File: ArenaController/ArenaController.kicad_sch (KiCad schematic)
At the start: 26 parts, among them J1 RJ45, J2 RJ45, J4 RJ45, J5 RJ45, J6 RJ45, J9 Barrel_Jack_MountingPin, Q1 FS3400, Q2 FS3400, Q3 FS3400, Q4 FS3400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

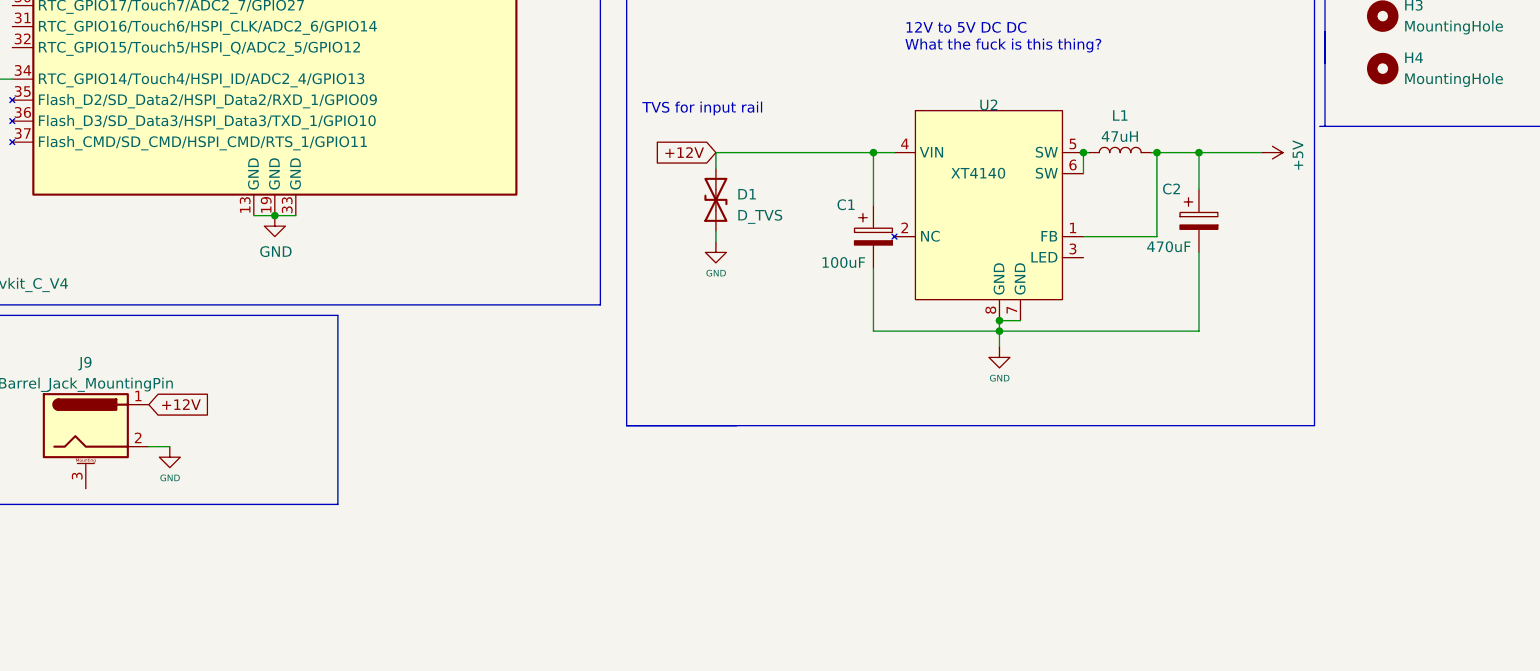
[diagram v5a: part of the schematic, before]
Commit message: Added test points and 3D model for pin headers to the ESP32 footprint.
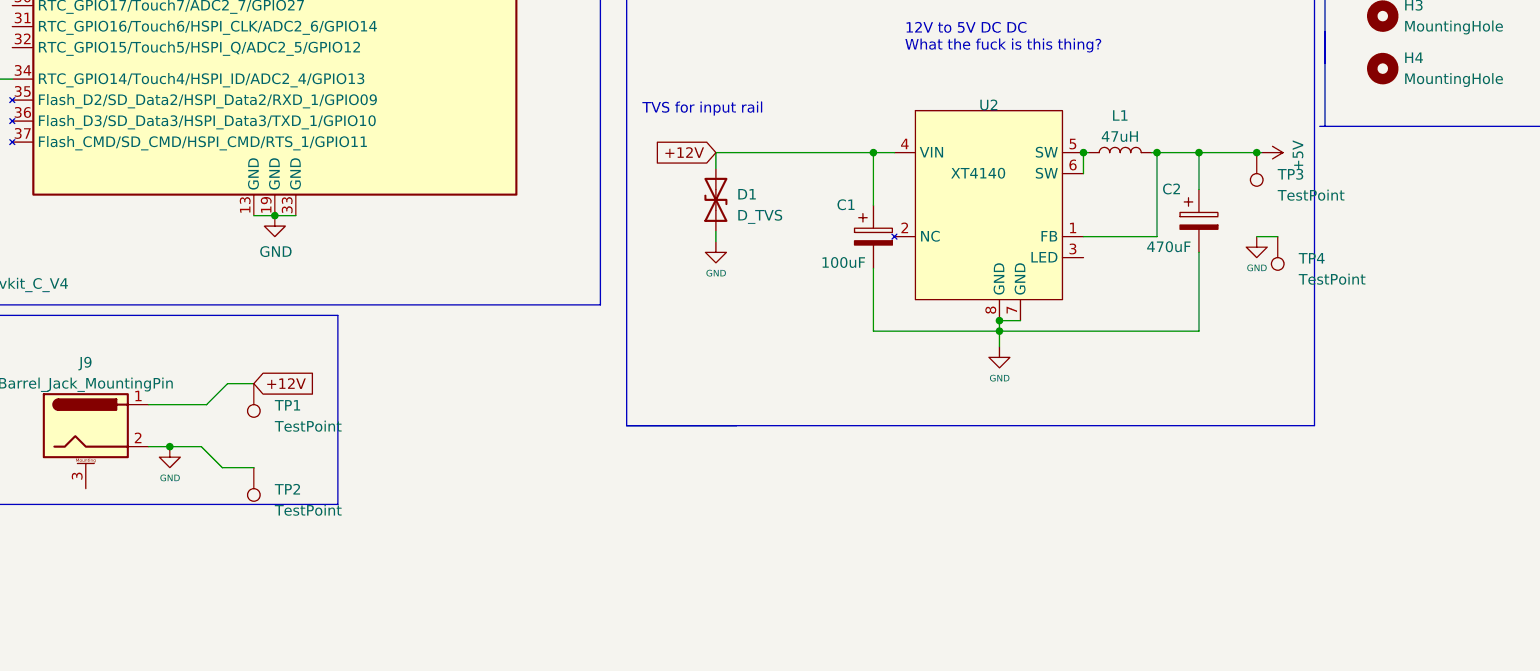
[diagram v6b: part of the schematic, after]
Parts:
- added TP1, TP2, TP3, TP4: TestPoint, TestPoint:TestPoint_Loop_D1.80mm_Drill1.0mm_Beaded, symbol Connector:TestPoint
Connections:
- net +12V: now also TP1.1
- net +5V: now also TP3.1
- net GND: now also TP2.1, TP4.1
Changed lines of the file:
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@@
   (title_block
     (title "Combat Arena Timing Control")
-    (date "2023-04-29")
-    (rev "0.5")
+    (date "2023-06-18")
+    (rev "0.6")
     (company "Fair Use Building & Research Labs, 501c3")
     (comment 2 "Neil Flynn")
@@
   (junction (at 172.085 123.825) (diameter 0) (color 0 0 0 0)
   )
+  (junction (at 47.625 159.385) (diameter 0) (color 0 0 0 0)
+  )
   (junction (at 147.955 144.145) (diameter 0) (color 0 0 0 0)
   )
   (junction (at 60.325 131.445) (diameter 0) (color 0 0 0 0)
   )
+  (junction (at 179.07 123.825) (diameter 0) (color 0 0 0 0)
+  )
   (junction (at 132.715 123.825) (diameter 0) (color 0 0 0 0)
   )
@@
     (stroke (width 0) (type default))
   )
-  (wire (pts (xy 172.085 123.825) (xy 179.705 123.825))
+  (wire (pts (xy 172.085 123.825) (xy 179.07 123.825))
     (stroke (width 0) (type default))
   )
@@
     (stroke (width 0) (type default))
   )
+  (wire (pts (xy 179.07 133.985) (xy 181.61 133.985))
+    (stroke (width 0) (type default))
+  )
   (wire (pts (xy 132.715 145.415) (xy 147.955 145.415))
     (stroke (width 0) (type default))
@@
     (stroke (width 0) (type default))
   )
+  (wire (pts (xy 53.975 161.925) (xy 57.785 161.925))
+    (stroke (width 0) (type default))
+  )
   (polyline (pts (xy 102.87 104.775) (xy 186.055 104.775))
     (stroke (width 0) (type default))
   )
+  (wire (pts (xy 54.61 151.765) (xy 57.785 151.765))
+    (stroke (width 0) (type default))
+  )
   (polyline (pts (xy 187.325 15.24) (xy 187.325 62.23))
     (stroke (width 0) (type default))
@@
     (stroke (width 0) (type default))
   )
+  (wire (pts (xy 47.625 159.385) (xy 51.435 159.385))
+    (stroke (width 0) (type default))
+  )
+  (wire (pts (xy 45.085 154.305) (xy 52.07 154.305))
+    (stroke (width 0) (type default))
+  )
   (polyline (pts (xy 187.325 113.03) (xy 187.325 109.22))
     (stroke (width 0) (type default))
@@
     (stroke (width 0) (type default))
   )
+  (wire (pts (xy 52.07 154.305) (xy 54.61 151.765))
+    (stroke (width 0) (type default))
+  )
   (polyline (pts (xy 118.11 102.87) (xy 153.67 102.87))
     (stroke (width 0) (type default))
@@
     (stroke (width 0) (type default))
   )
+  (wire (pts (xy 179.07 123.825) (xy 179.705 123.825))
+    (stroke (width 0) (type default))
+  )
   (wire (pts (xy 170.18 57.15) (xy 168.91 57.15))
     (stroke (width 0) (type default))
   )
   (wire (pts (xy 26.035 74.295) (xy 28.575 74.295))
+    (stroke (width 0) (type default))
+  )
+  (wire (pts (xy 51.435 159.385) (xy 53.975 161.925))
     (stroke (width 0) (type default))
   )
@@
     )
   )
-  (global_label "+12V" (shape input) (at 45.085 154.305 0) (fields_autoplaced)
+  (global_label "+12V" (shape input) (at 57.785 151.765 0) (fields_autoplaced)
     (effects (font (size 1.27 1.27)) (justify left))
-    (property "Intersheetrefs" "${INTERSHEET_REFS}" (at 52.4892 154.3844 0)
+    (property "Intersheetrefs" "${INTERSHEET_REFS}" (at 65.1892 151.8444 0)
       (effects (font (size 1.27 1.27)) (justify left) hide)
     )
@@
     )
   )
+  (symbol (lib_id "Connector:TestPoint") (at 179.07 123.825 180) (unit 1)
+    (in_bom yes) (on_board yes) (dnp no) (fields_autoplaced)
+    (property "Reference" "TP3" (at 181.61 126.492 0)
+      (effects (font (size 1.27 1.27)) (justify right))
+    )
+    (property "Value" "TestPoint" (at 181.61 129.032 0)
+      (effects (font (size 1.27 1.27)) (justify right))
+    )
+    (property "Footprint" "TestPoint:TestPoint_Loop_D1.80mm_Drill1.0mm_Beaded" (at 173.99 123.825 0)
+      (effects (font (size 1.27 1.27)) hide)
+    )
+    (property "Datasheet" "~" (at 173.99 123.825 0)
+      (effects (font (size 1.27 1.27)) hide)
+    )
+    (pin "1")
+    (instances
+      (project "ArenaController"
+        (path "/156576da-4c7a-4c71-af43-7540e3a24bd3"
+          (reference "TP3") (unit 1)
+        )
+      )
+    )
+  )
   (symbol (lib_id "Device:D_TVS") (at 113.665 129.54 90) (unit 1)
     (in_bom yes) (on_board yes) (dnp no) (fields_autoplaced)
@@
         (path "/156576da-4c7a-4c71-af43-7540e3a24bd3"
           (reference "R5") (unit 1)
+        )
+      )
+    )
+  )
+  (symbol (lib_id "Connector:TestPoint") (at 57.785 161.925 180) (unit 1)
+    (in_bom yes) (on_board yes) (dnp no) (fields_autoplaced)
+    (property "Reference" "TP2" (at 60.325 164.592 0)
+      (effects (font (size 1.27 1.27)) (justify right))
+    )
+    (property "Value" "TestPoint" (at 60.325 167.132 0)
+      (effects (font (size 1.27 1.27)) (justify right))
+    )
+    (property "Footprint" "TestPoint:TestPoint_Loop_D1.80mm_Drill1.0mm_Beaded" (at 52.705 161.925 0)
+      (effects (font (size 1.27 1.27)) hide)
+    )
+    (property "Datasheet" "~" (at 52.705 161.925 0)
+      (effects (font (size 1.27 1.27)) hide)
+    )
+    (pin "1")
+    (instances
+      (project "ArenaController"
+        (path "/156576da-4c7a-4c71-af43-7540e3a24bd3"
+          (reference "TP2") (unit 1)
         )
       )
@@
     )
   )
+  (symbol (lib_id "Connector:TestPoint") (at 181.61 133.985 180) (unit 1)
+    (in_bom yes) (on_board yes) (dnp no) (fields_autoplaced)
+    (property "Reference" "TP4" (at 184.15 136.652 0)
+      (effects (font (size 1.27 1.27)) (justify right))
+    )
+    (property "Value" "TestPoint" (at 184.15 139.192 0)
+      (effects (font (size 1.27 1.27)) (justify right))
+    )
+    (property "Footprint" "TestPoint:TestPoint_Loop_D1.80mm_Drill1.0mm_Beaded" (at 176.53 133.985 0)
+      (effects (font (size 1.27 1.27)) hide)
+    )
+    (property "Datasheet" "~" (at 176.53 133.985 0)
+      (effects (font (size 1.27 1.27)) hide)
+    )
+    (pin "1")
+    (instances
+      (project "ArenaController"
+        (path "/156576da-4c7a-4c71-af43-7540e3a24bd3"
+          (reference "TP4") (unit 1)
+        )
+      )
+    )
+  )
   (symbol (lib_id "power:GND") (at 201.93 73.66 0) (unit 1)
     (in_bom yes) (on_board yes) (dnp no)
@@
     )
   )
+  (symbol (lib_id "Connector:TestPoint") (at 57.785 151.765 180) (unit 1)
+    (in_bom yes) (on_board yes) (dnp no) (fields_autoplaced)
+    (property "Reference" "TP1" (at 60.325 154.432 0)
+      (effects (font (size 1.27 1.27)) (justify right))
+    )
+    (property "Value" "TestPoint" (at 60.325 156.972 0)
+      (effects (font (size 1.27 1.27)) (justify right))
+    )
+    (property "Footprint" "TestPoint:TestPoint_Loop_D1.80mm_Drill1.0mm_Beaded" (at 52.705 151.765 0)
+      (effects (font (size 1.27 1.27)) hide)
+    )
+    (property "Datasheet" "~" (at 52.705 151.765 0)
+      (effects (font (size 1.27 1.27)) hide)
+    )
+    (pin "1")
+    (instances
+      (project "ArenaController"
+        (path "/156576da-4c7a-4c71-af43-7540e3a24bd3"
+          (reference "TP1") (unit 1)
+        )
+      )
+    )
+  )
   (symbol (lib_id "power:+5V") (at 179.705 123.825 270) (unit 1)
     (in_bom yes) (on_board yes) (dnp no)
@@
         )
       )
+    )
+  )
+  (symbol (lib_id "power:GND") (at 179.07 133.985 0) (unit 1)
+    (in_bom yes) (on_board yes) (dnp no)
+    (property "Reference" "#PWR03" (at 179.07 140.335 0)
+      (effects (font (size 0.7874 0.7874)) hide)
+    )
+    (property "Value" "GND" (at 180.34 137.795 0)
+      (effects (font (size 0.7874 0.7874)) (justify right))
+    )
+    (property "Footprint" "" (at 179.07 133.985 0)
+      (effects (font (size 1.27 1.27)) hide)
+    )
+    (property "Datasheet" "" (at 179.07 133.985 0)
+      (effects (font (size 1.27 1.27)) hide)
+    )
+    (pin "1")
+    (instances
+      (project "ArenaController"
+        (path "/156576da-4c7a-4c71-af43-7540e3a24bd3"
+          (reference "#PWR03") (unit 1)
+        )
+      )

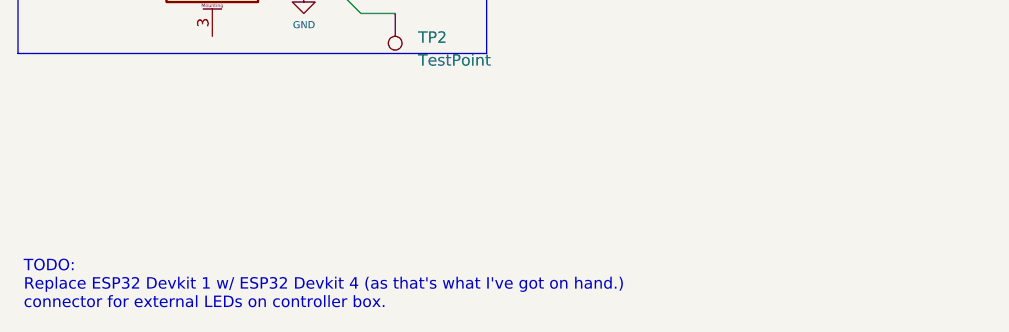
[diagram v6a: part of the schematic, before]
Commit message: Updated arena controls, delete team signs that are now deprecated, added more footprints.
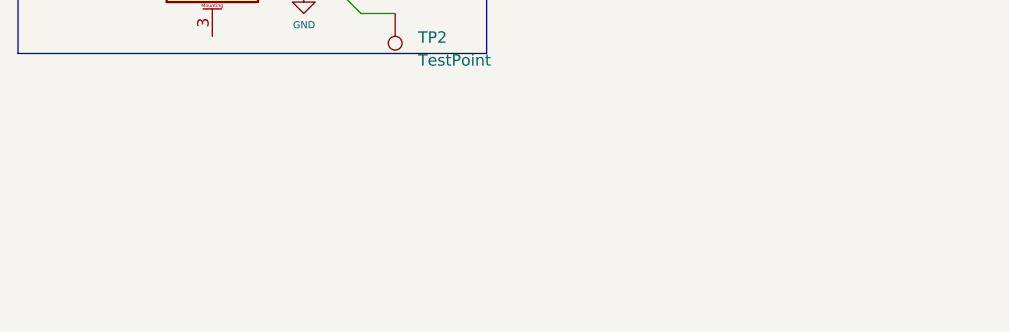
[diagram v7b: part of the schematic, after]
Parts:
- C1: LCSC (none) -> https://www.lcsc.com/product-detail/Aluminum-Electrolytic-C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
- C2: footprint Capacitor_SMD:C_Elec_6.3x5.4 -> Capacitor_SMD:C_Elec_6.3x7.7
- Q3: LCSC (none) -> https://www.lcsc.com/product-detail/MOSFETs_FOSAN-FS3400_C2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
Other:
- note removed: "TODO: Replace ESP32 Devkit 1 w/ ESP32 Devkit 4 (as that's what I've got on hand.) connector for external LEDs on controller box."
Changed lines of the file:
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@@
   (title_block
     (title "Combat Arena Timing Control")
-    (date "2023-06-18")
+    (date "2023-06-19")
     (rev "0.6")
     (company "Fair Use Building & Research Labs, 501c3")
@@
     (effects (font (size 1.27 1.27)) (justify left bottom))
   )
-  (text "TODO:\nReplace ESP32 Devkit 1 w/ ESP32 Devkit 4 (as that's what I've got on hand.)\nconnector for external LEDs on controller box."
-    (at 16.51 194.945 0)
-    (effects (font (size 1.27 1.27)) (justify left bottom))
-  )
   (text "Team 2 Stacklight" (at 194.31 50.8 0)
     (effects (font (size 1.27 1.27)) (justify left bottom))
@@
       (effects (font (size 1.27 1.27)) hide)
     )
+    (property "LCSC" "https://www.lcsc.com/product-detail/MOSFETs_FOSAN-FS3400_C2926126.html" (at 142.24 30.48 0)
+      (effects (font (size 1.27 1.27)) hide)
+    )
     (pin "1")
     (pin "2")
@@
       (effects (font (size 1.27 1.27)) hide)
     )
-    (property "Datasheet" "" (at 130.81 86.36 0)
+    (property "Datasheet" "https://datasheet.lcsc.com/lcsc/2205311900_UNI-ROYAL-Uniroyal-Elec-1206W4J0331T5E_C25374.pdf" (at 130.81 86.36 0)
       (effects (font (size 1.27 1.27)) hide)
     )
@@
       (effects (font (size 1.27 1.27)) hide)
     )
-    (property "Datasheet" "" (at 133.35 30.48 0)
+    (property "Datasheet" "https://datasheet.lcsc.com/lcsc/2205311900_UNI-ROYAL-Uniroyal-Elec-1206W4J0331T5E_C25374.pdf" (at 133.35 30.48 0)
       (effects (font (size 1.27 1.27)) hide)
     )
@@
       (effects (font (size 1.27 1.27)) hide)
     )
+    (property "LCSC" "https://www.lcsc.com/product-detail/Aluminum-Electrolytic-Capacitors-SMD_KNSCHA-RST100UF25V004_C4747964.html" (at 132.715 133.985 0)
+      (effects (font (size 1.27 1.27)) hide)
+    )
     (pin "1")
     (pin "2")
@@
       (effects (font (size 1.27 1.27)) hide)
     )
-    (property "Datasheet" "" (at 162.56 123.825 0)
+    (property "Datasheet" "https://datasheet.lcsc.com/lcsc/2304140030_TDK-NLV32T-470J-PF_C66936.pdf" (at 162.56 123.825 0)
       (effects (font (size 1.27 1.27)) hide)
     )
@@
       (effects (font (size 1.27 1.27)) hide)
     )
-    (property "Datasheet" "" (at 166.37 57.15 0)
+    (property "Datasheet" "https://datasheet.lcsc.com/lcsc/2205311900_UNI-ROYAL-Uniroyal-Elec-1206W4J0331T5E_C25374.pdf" (at 166.37 57.15 0)
       (effects (font (size 1.27 1.27)) hide)
     )
@@
       (effects (font (size 1.27 1.27)) hide)
     )
-    (property "Datasheet" "" (at 163.83 30.48 0)
+    (property "Datasheet" "https://datasheet.lcsc.com/lcsc/2205311900_UNI-ROYAL-Uniroyal-Elec-1206W4J0331T5E_C25374.pdf" (at 163.83 30.48 0)
       (effects (font (size 1.27 1.27)) hide)
     )
@@
       (effects (font (size 1.27 1.27)) (justify left))
     )
-    (property "Footprint" "Capacitor_SMD:C_Elec_6.3x5.4" (at 173.0502 135.89 0)
-      (effects (font (size 1.27 1.27)) hide)
-    )
-    (property "Datasheet" "https://datasheet.lcsc.com/lcsc/2202231130_ROQANG-RVT1C471M0607_C2977552.pdf" (at 172.085 132.08 0)
+    (property "Footprint" "Capacitor_SMD:C_Elec_6.3x7.7" (at 173.0502 135.89 0)
+      (effects (font (size 1.27 1.27)) hide)
+    )
+    (property "Datasheet" "~" (at 172.085 132.08 0)
       (effects (font (size 1.27 1.27)) hide)
     )
@@
       (effects (font (size 1.27 1.27)) hide)
     )
-    (property "Datasheet" "" (at 133.35 57.15 0)
-      (effects (font (size 1.27 1.27)) hide)
-    )
+    (property "Datasheet" "https://datasheet.lcsc.com/lcsc/2205311900_UNI-ROYAL-Uniroyal-Elec-1206W4J0331T5E_C25374.pdf" (at 133.35 57.15 0)
+      (effects (font (size 1.27 1.27)) hide)
+    )

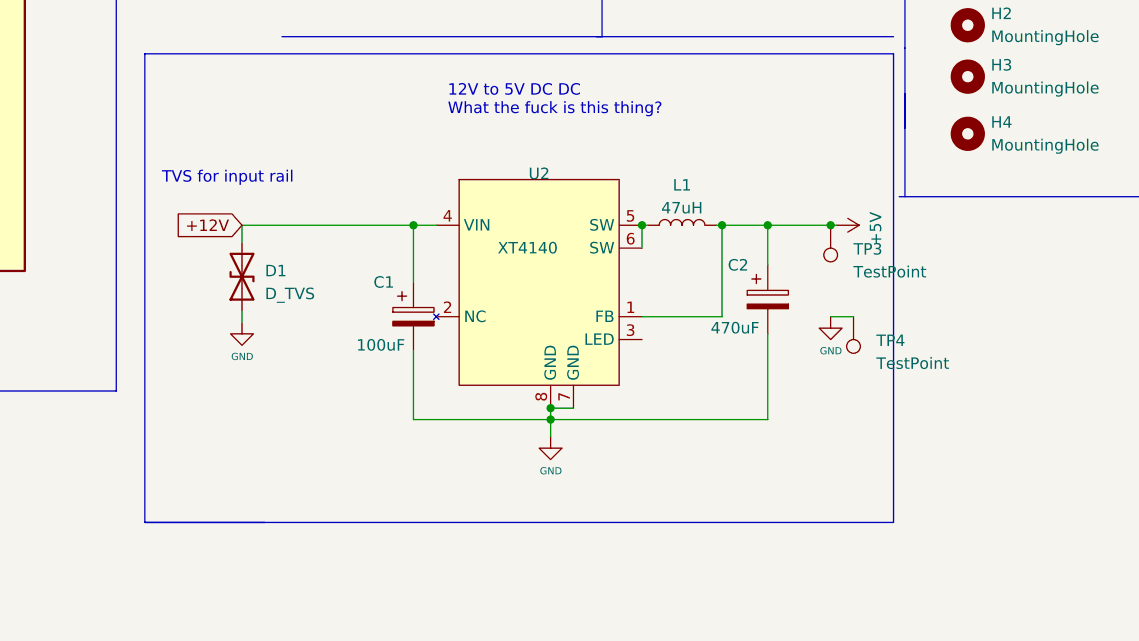
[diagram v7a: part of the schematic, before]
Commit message: Changed output tool to fix missing drill files, at least in theory.
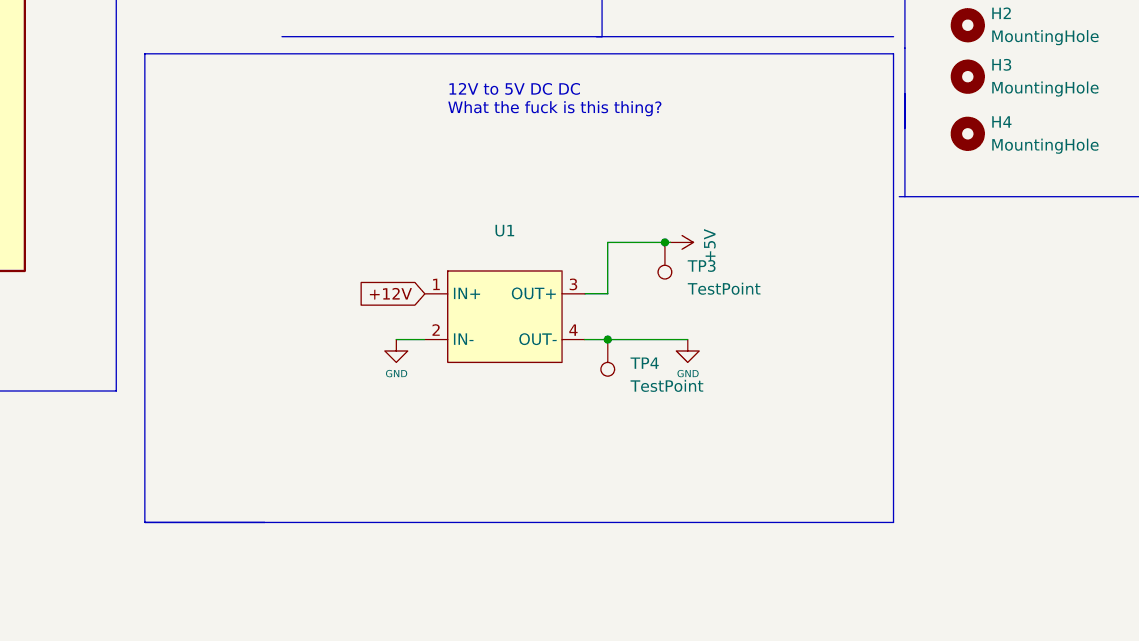
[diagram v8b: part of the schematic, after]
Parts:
- removed C1: 100uF, Capacitor_SMD:C_Elec_6.3x5.4, symbol Device:C_Polarized
- removed C2: 470uF, Capacitor_SMD:C_Elec_6.3x7.7, symbol Device:C_Polarized
- removed D1: D_TVS, Diode_SMD:D_SOD-123F, symbol Device:D_TVS
- removed L1: 47uH, Inductor_SMD:L_1210_3225Metric_Pad1.42x2.65mm_HandSolder, symbol Device:L
- removed U2: XT4140, Package_SO:SOP-8_3.76x4.96mm_P1.27mm, symbol symbols:TX4140
- added U1: ~, footprints:LM2596_Module, symbol symbols:LM2596_Module
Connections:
- net +12V: now also U1.1 (IN+)
- net +5V: now also U1.3 (OUT+)
- net GND: now also U1.2 (IN-), U1.4 (OUT-)
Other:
- note removed: "TVS for input rail"
- moved on the sheet: TP3, TP4
